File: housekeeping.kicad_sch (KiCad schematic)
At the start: 20 parts

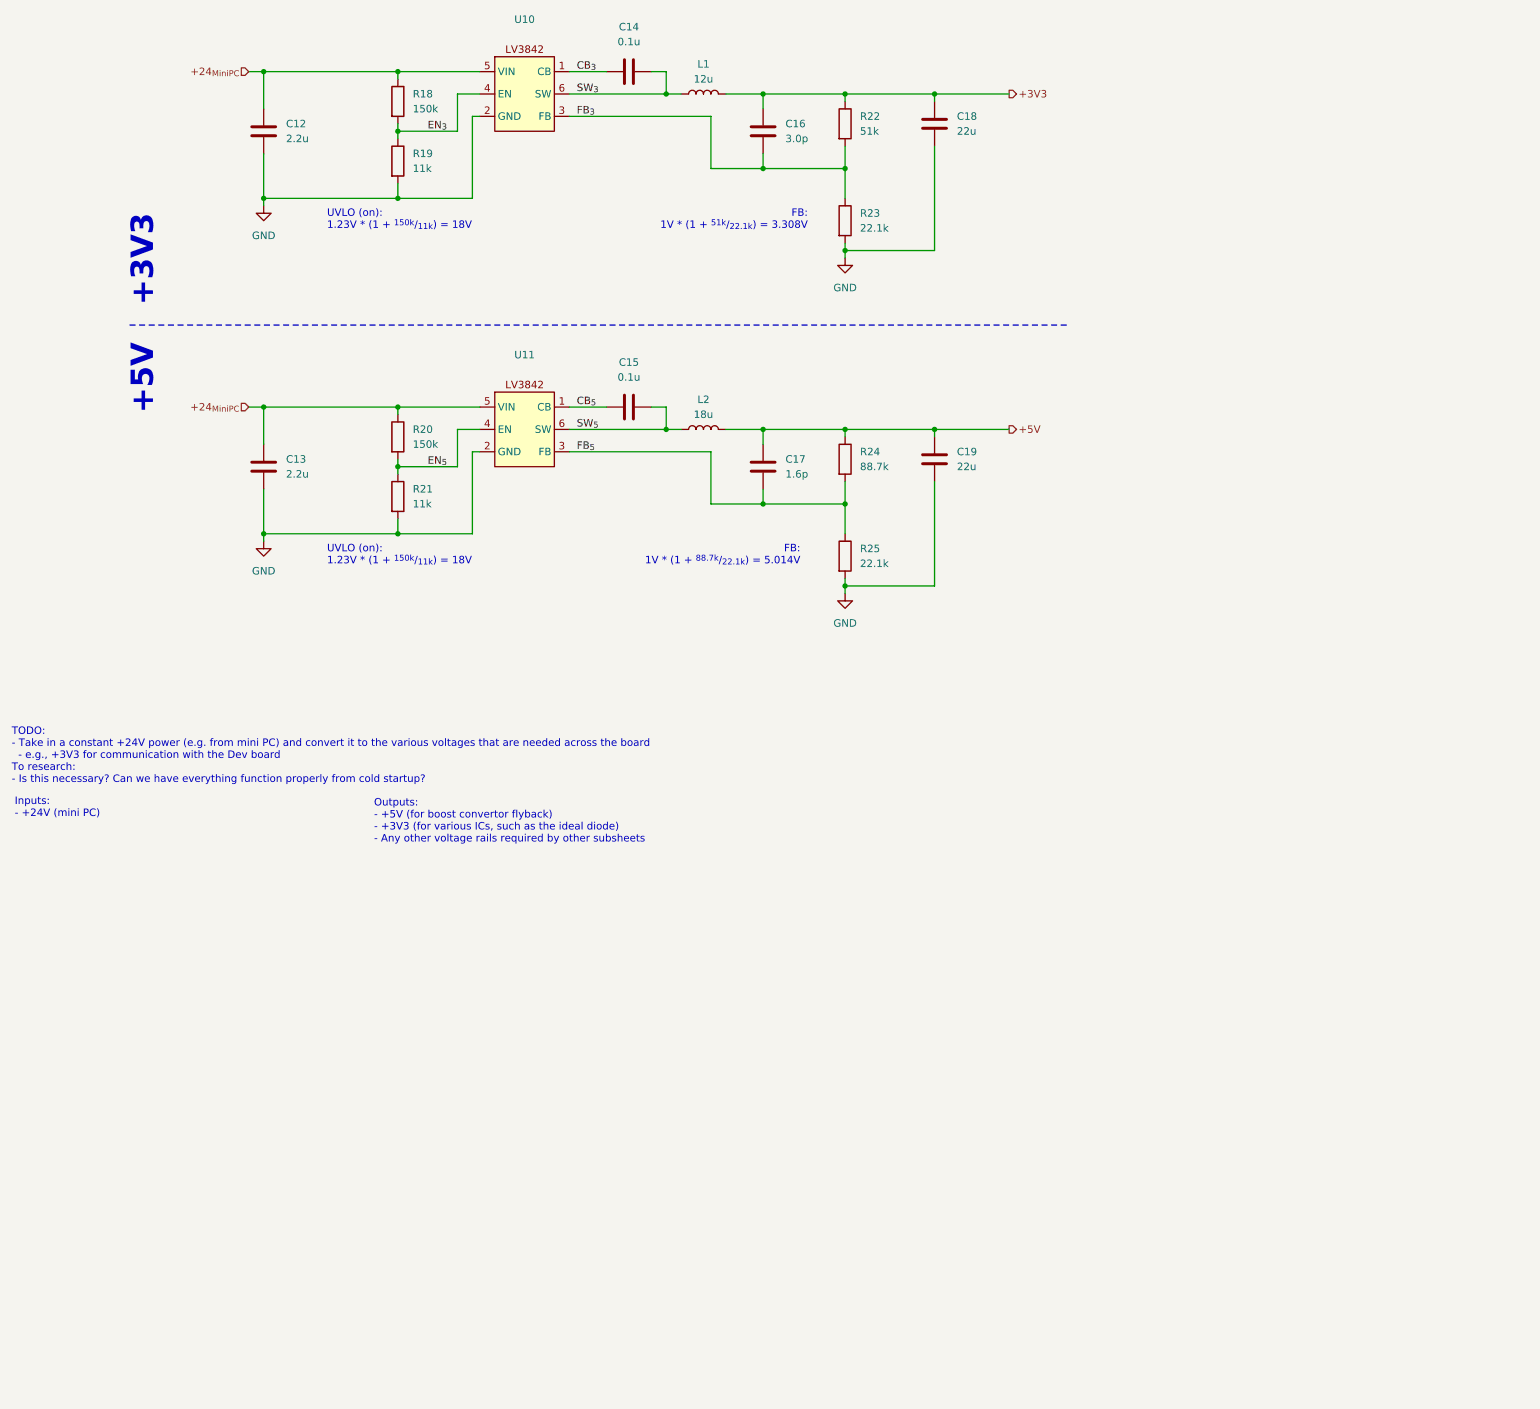
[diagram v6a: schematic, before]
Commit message: Add in voltage control for components
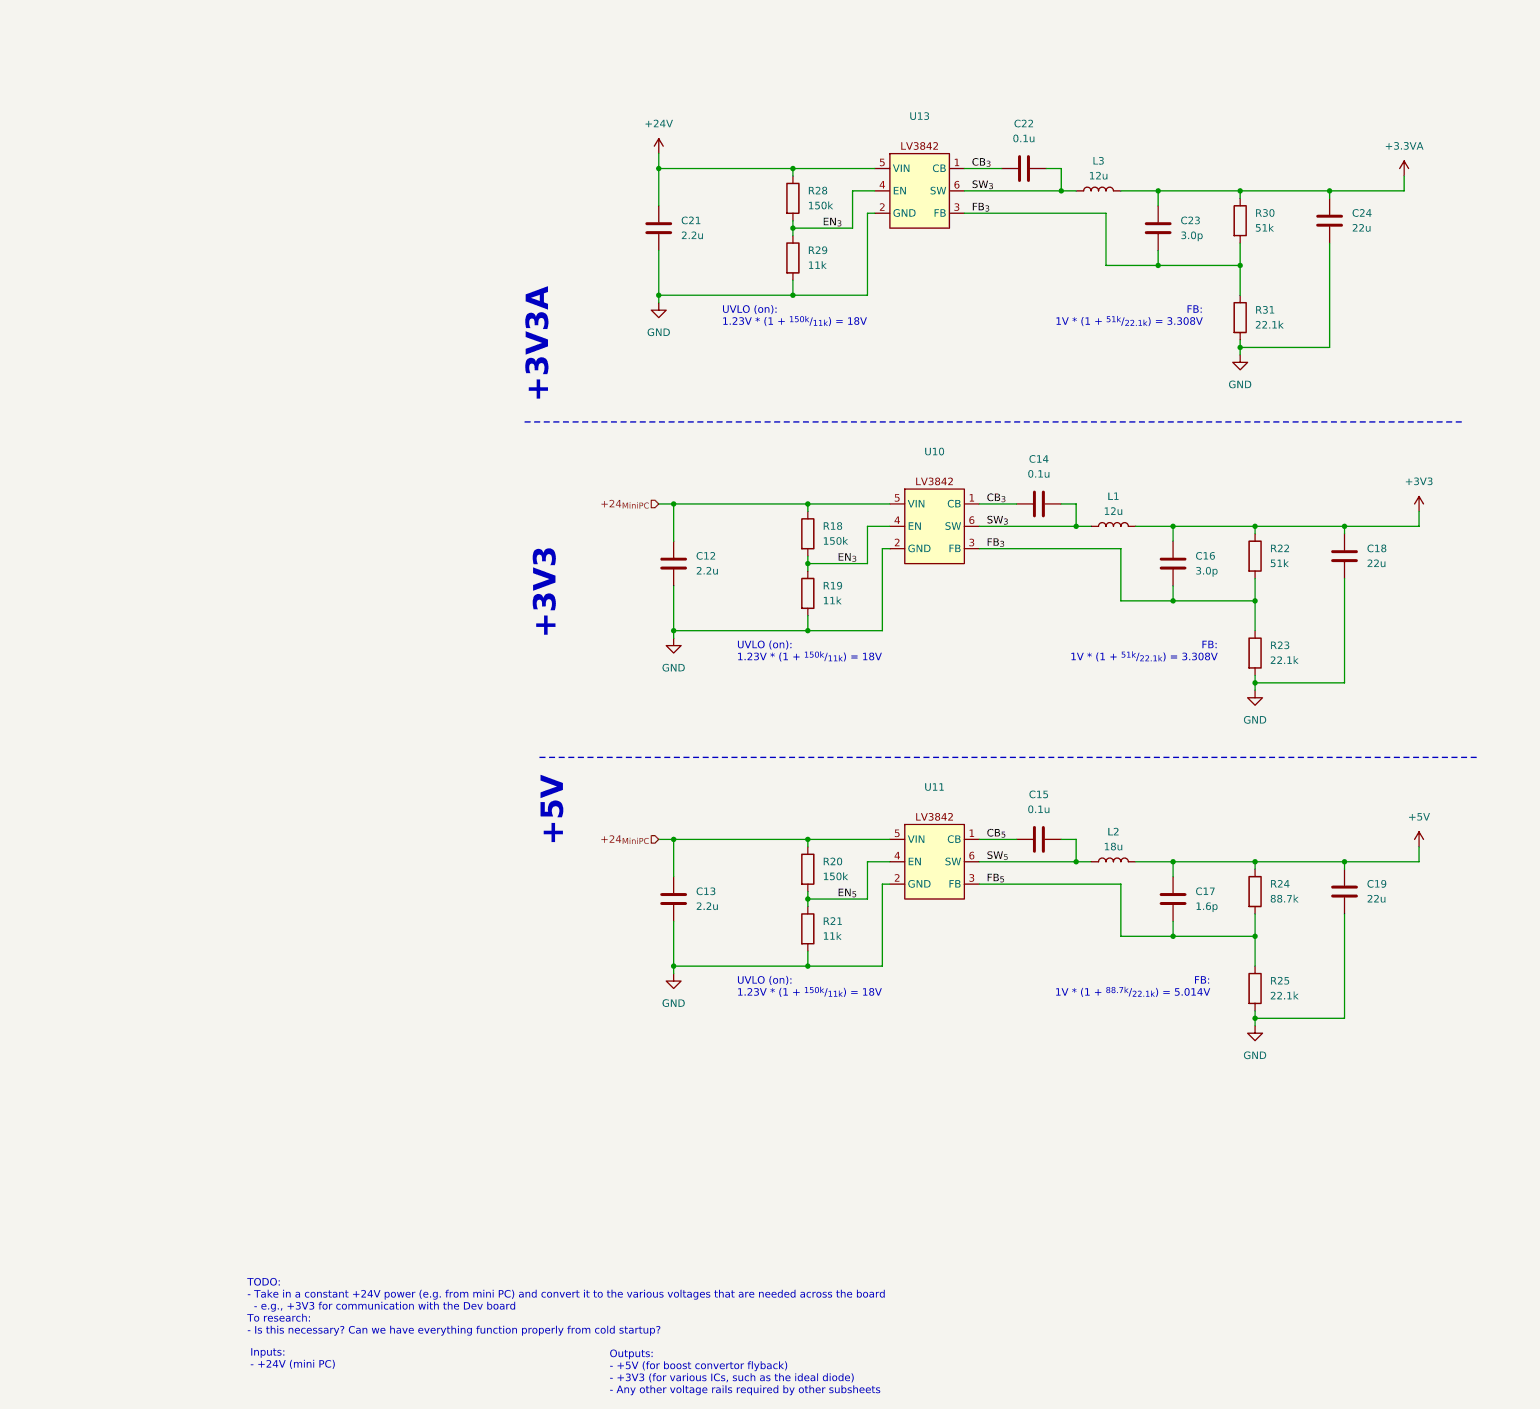
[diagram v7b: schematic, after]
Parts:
- added C21: 2.2u, Capacitor_SMD:C_0603_1608Metric_Pad1.08x0.95mm_HandSolder, symbol Device:C
- added C22: 0.1u, Capacitor_SMD:C_0603_1608Metric_Pad1.08x0.95mm_HandSolder, symbol Device:C
- added C23: 3.0p, Capacitor_SMD:C_0603_1608Metric_Pad1.08x0.95mm_HandSolder, symbol Device:C
- added C24: 22u, Capacitor_SMD:C_0603_1608Metric_Pad1.08x0.95mm_HandSolder, symbol Device:C
- added L3: 12u, symbol Device:L
- added R28: 150k, Resistor_SMD:R_0603_1608Metric_Pad0.98x0.95mm_HandSolder, symbol Device:R
- added R29: 11k, Resistor_SMD:R_0603_1608Metric_Pad0.98x0.95mm_HandSolder, symbol Device:R
- added R30: 51k, Resistor_SMD:R_0603_1608Metric_Pad0.98x0.95mm_HandSolder, symbol Device:R
- added R31: 22.1k, Resistor_SMD:R_0603_1608Metric_Pad0.98x0.95mm_HandSolder, symbol Device:R
- added U13: ~, Package_TO_SOT_SMD:SOT-23-6_Handsoldering, symbol ! Robomaster ICs:LV3842
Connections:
- net CB_{3}: now also C22.1, U13.1 (CB)
- net EN_{3}: now also R28.2, R29.1, U13.4 (EN)
- net FB_{3}: now also C23.1, R30.2, R31.1, U13.3 (FB)
- net GND: now also C21.2, C24.2, R29.2, R31.2, U13.2 (GND)
- net SW_{3}: now also C22.2, L3.1, U13.6 (SW)
- new net +24V: C21.1, R28.1, U13.5 (VIN)
- new net +3.3VA: C23.2, C24.1, L3.2, R30.1
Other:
- note added: "+3V3A"
- moved on the sheet: C12, C13, C14, C15, C16, C17, C18, C19, L1, L2, R18, R19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

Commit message: Define feedback networks
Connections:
- net CB_{3}: no longer C22.1, U13.1 (CB)
- net EN_{3}: no longer R28.2, R29.1, U13.4 (EN)
- net FB_{3}: no longer C23.1, R30.2, R31.1, U13.3 (FB)
- net SW_{3}: no longer C22.2, L3.1, U13.6 (SW)
- new net CB_{3A}: C22.1, U13.1 (CB)
- new net EN_{3A}: R28.2, R29.1, U13.4 (EN)
- new net FB_{3A}: C23.1, R30.2, R31.1, U13.3 (FB)
- new net SW_{3A}: C22.2, L3.1, U13.6 (SW)
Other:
- note added: "Ripple network design follows https://www.ti.com/lit/an/snva776a/snva776a.pdf?ts=1733621536294&ref_url=https%253A%252F%252Fduckduckgo.com%252F"
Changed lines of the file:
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@@
+		)
+	)
+	(text "Ripple network design follows https://www.ti.com/lit/an/snva776a/snva776a.pdf?ts=1733621536294&ref_url=https%253A%252F%252Fduckduckgo.com%252F"
+		(exclude_from_sim no)
+		(at 213.106 224.282 0)
+		(effects
+			(font
+				(size 1.27 1.27)
+			)
 		)
 	)
@@
 		)
 	)
-	(label "FB_{3}"
+	(label "FB_{3A}"
 		(at 208.28 73.66 0)
 		(fields_autoplaced yes)
@@
 		)
 	)
-	(label "EN_{3}"
+	(label "EN_{3A}"
 		(at 182.88 76.2 0)
 		(fields_autoplaced yes)
@@
 		)
 	)
-	(label "CB_{3}"
+	(label "CB_{3A}"
 		(at 208.28 66.04 0)
 		(fields_autoplaced yes)
@@
 		)
 	)
-	(label "SW_{3}"
+	(label "SW_{3A}"
 		(at 208.28 69.85 0)
 		(fields_autoplaced yes)
